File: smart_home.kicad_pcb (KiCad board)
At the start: 2 copper layers, 200 x 100 mm, 76 parts, among them J1A AC_IN_1, J1B AC_IN_2, J1C AC_IN_3, J1D AC_IN_4, J2A LOAD_1, J2B LOAD_2, J2C LOAD_3, J2D LOAD_4, J3 PROG, J4 LCD I2C, J5 V_SENSE_1, J6 V_SENSE_2, J7 V_SENSE_3, J8 V_SENSE_4, K1 SRD-05VDC-SL-C, K2 SRD-05VDC-SL-C, K3 SRD-05VDC-SL-C, K4 SRD-05VDC-SL-C, SW1 TACT_6mm, SW2 TACT_6mm, SW3 TACT_6mm, SW4 TACT_6mm, SW5 TACT_6mm, SW6 TACT_6mm, U1 ESP32-WROOM-32E, U2 ULN2003A, U3 AMS1117-3.3, U4 ACS712-05B, U5 ACS712-05B, U6 ACS712-05B, U7 ACS712-05B, U8 ADS1115

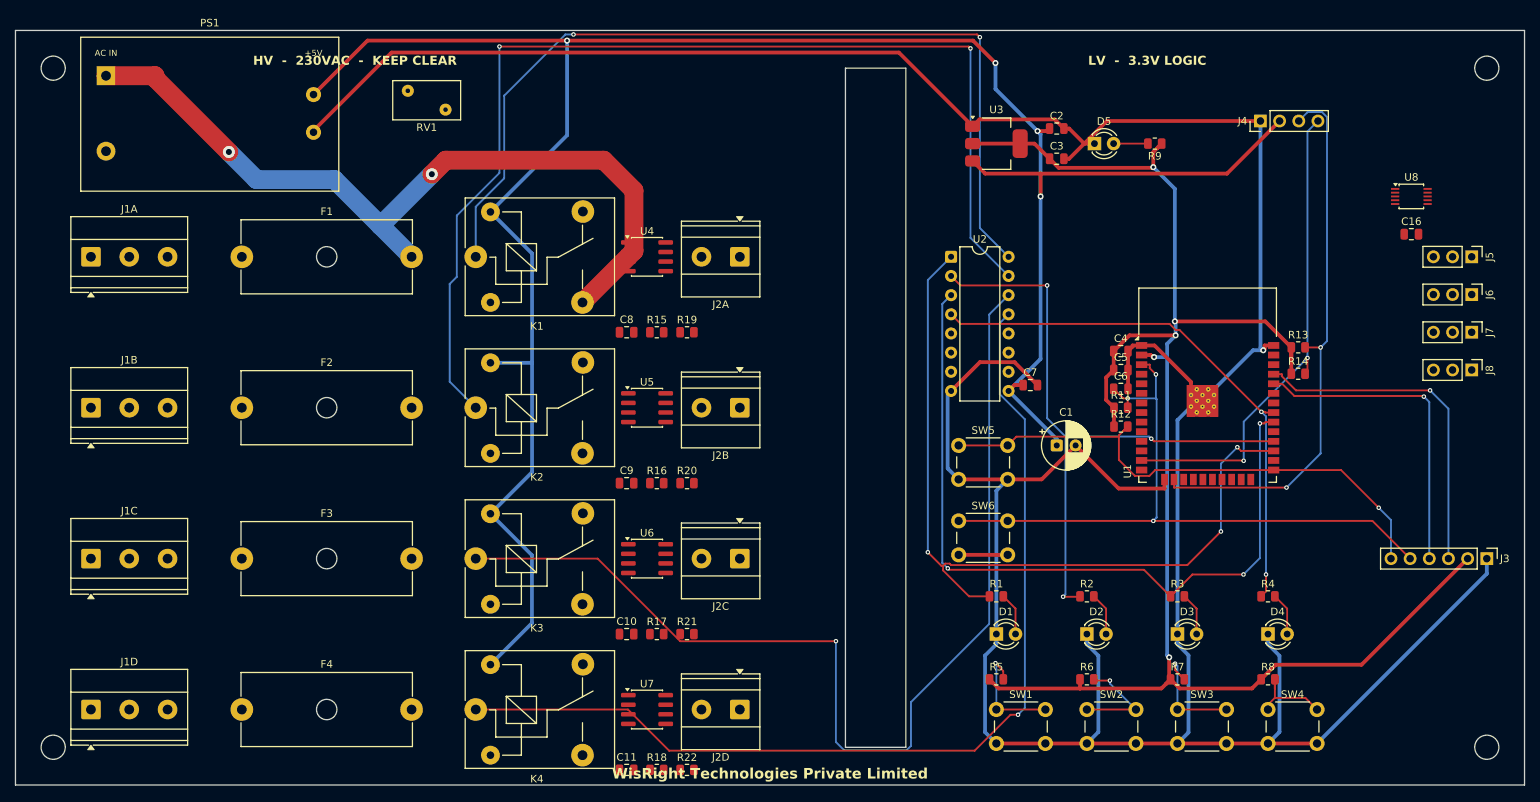
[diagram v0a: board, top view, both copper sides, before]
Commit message: Run Freerouting autoroute on updated PCB (post ACS712+ADS1115)
Process:
1. Pcbnew Python API: rip up all 426 stale tracks/42 vias from prior pass
   (they predated the ACS712 net-topology change and were inconsistent)
2. Export fresh Specctra DSN (smart_home.dsn)
3. Freerouting 1.9.0 batch autoroute, 50 passes, 4 threads
4. Import SES back via pcbnew.ImportSpecctraSES

Result: 368 segments + 28 vias placed across 32 nets.
DRC: 59 violations (36 clearance — Freerouting doesn't honor the custom
.kicad_dru HV clearance rule, so HV nets need a manual cleanup pass in
the PCB editor), plus 19 cosmetic (silk overlap, lib_footprint_mismatch).
Unconnected: 66 ratsnest items remain — mostly HV channel-internal nets
(L1_RAW-L4_RAW, N1-N4, PE chain, LOAD1-4 splits through ACS712) that
require the 2.5mm AC_HV trace width and 4mm clearance.

Fabrication outputs regenerated under fabrication/ + smart_home-fab.zip.
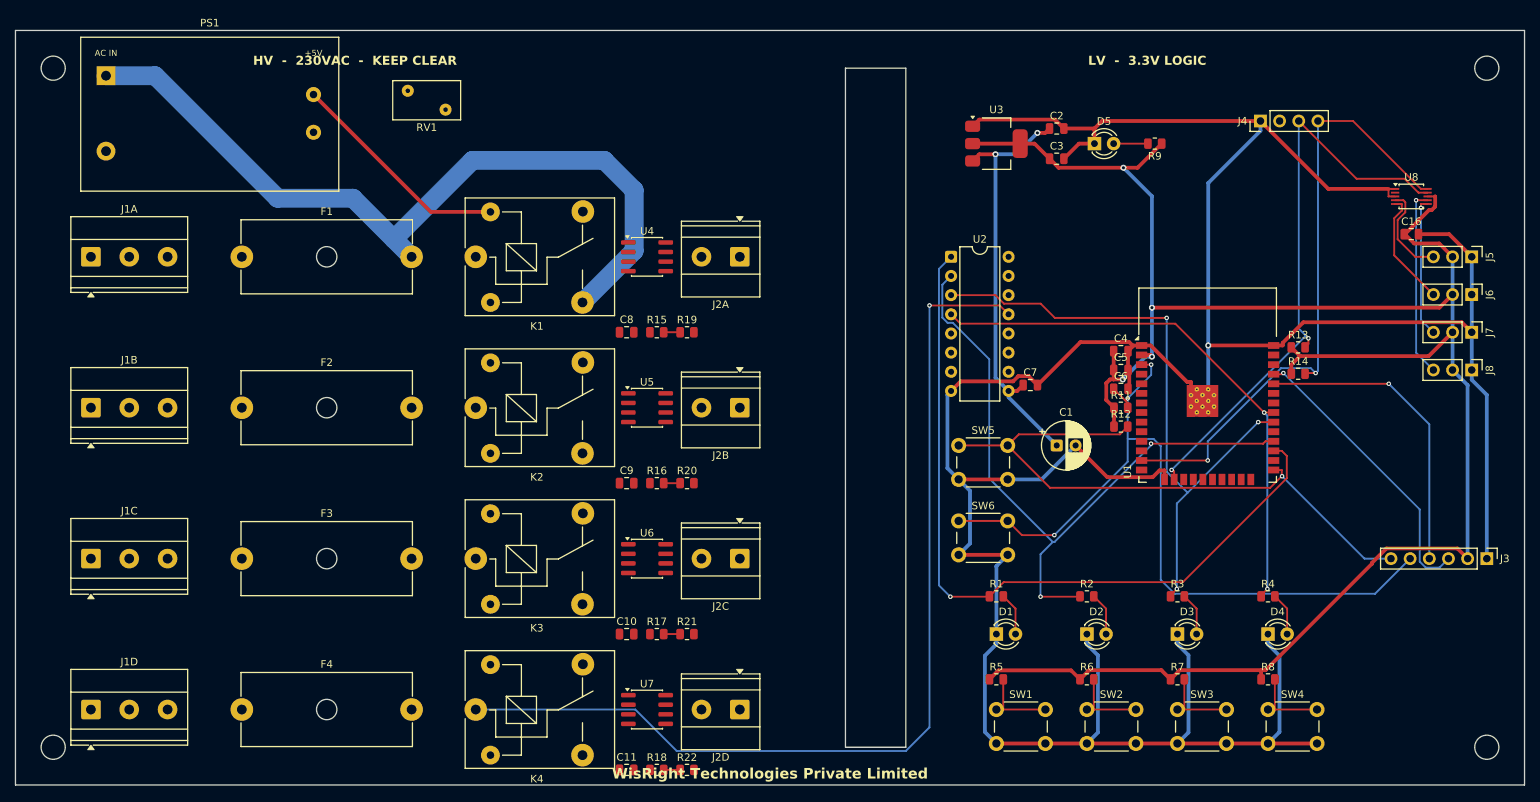
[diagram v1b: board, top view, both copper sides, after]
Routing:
- net +5V: track 305.0 -> 86.1 mm, vias 4 -> 2
- net COIL2: track 146.8 -> 0.00 mm, vias 2 -> 0
- net COIL3: track 141.4 -> 0.00 mm, vias 1 -> 0
- net COIL1: track 120.2 -> 0.00 mm, vias 2 -> 0
- net +3V3: track 218.8 -> 270.5 mm, vias 5 -> 4
- net GND: track 479.9 -> 436.2 mm
- net V_SENSE_4: track 0.00 -> 25.0 mm, vias 0 -> 1
- net V_SENSE_3: track 0.00 -> 18.6 mm, vias 0 -> 1
- net IO18: track 102.6 -> 84.1 mm
- net SCL_LCD: track 64.9 -> 83.1 mm
- net V_SENSE_2: track 0.00 -> 15.4 mm
- net EN: track 91.6 -> 104.6 mm
- net V_SENSE_1: track 0.00 -> 12.5 mm
- net IO0: track 72.6 -> 83.6 mm
- net TXD0: track 45.1 -> 38.5 mm
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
